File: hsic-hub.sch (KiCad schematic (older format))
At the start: 10 parts

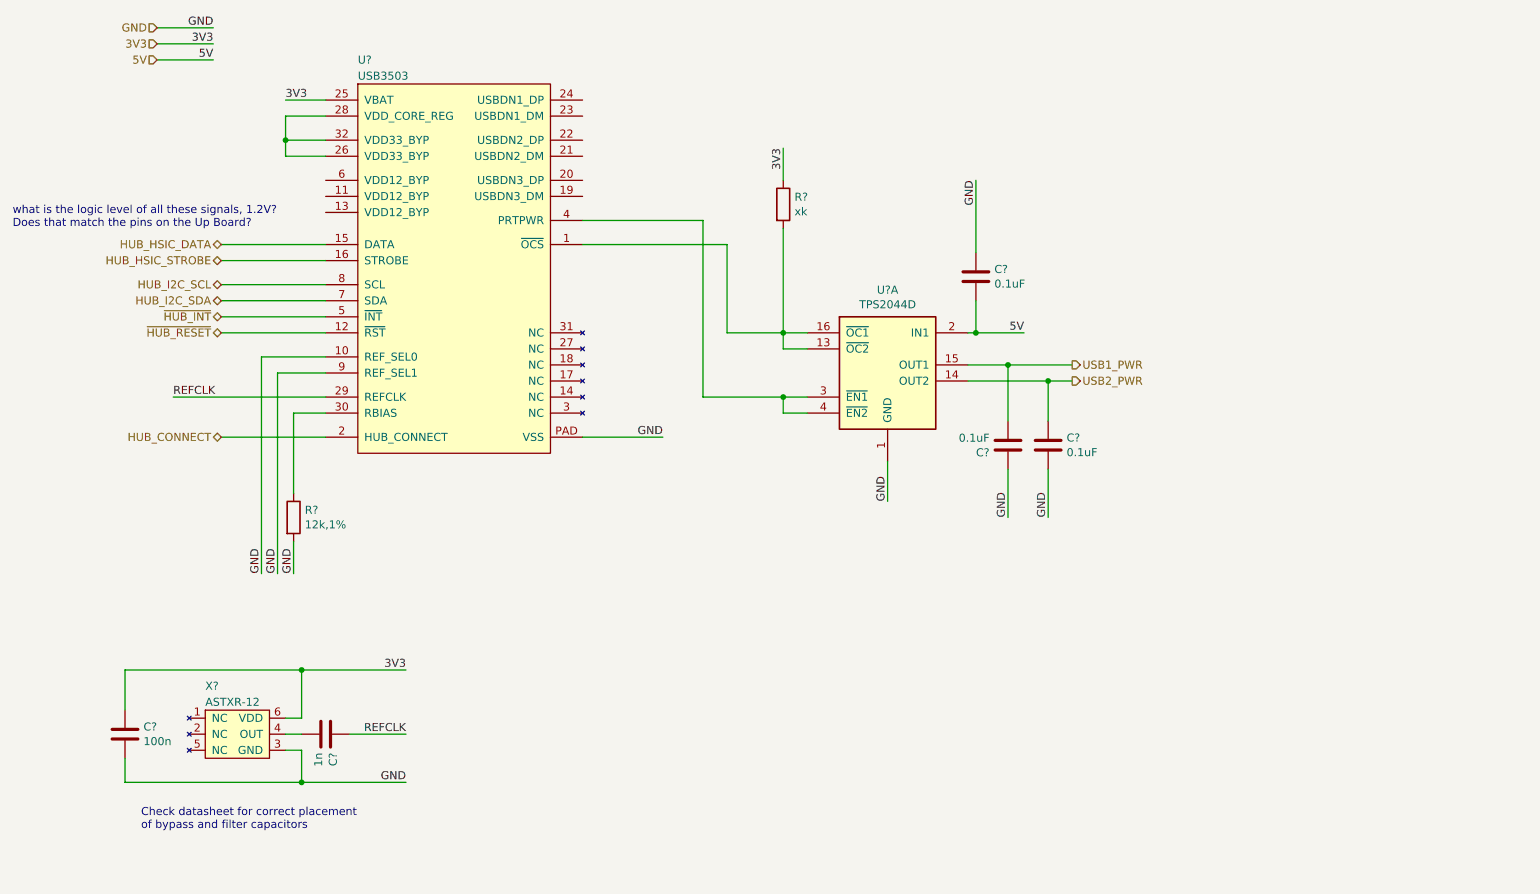
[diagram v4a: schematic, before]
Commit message: Add header for USB connector to libraries and schematic.
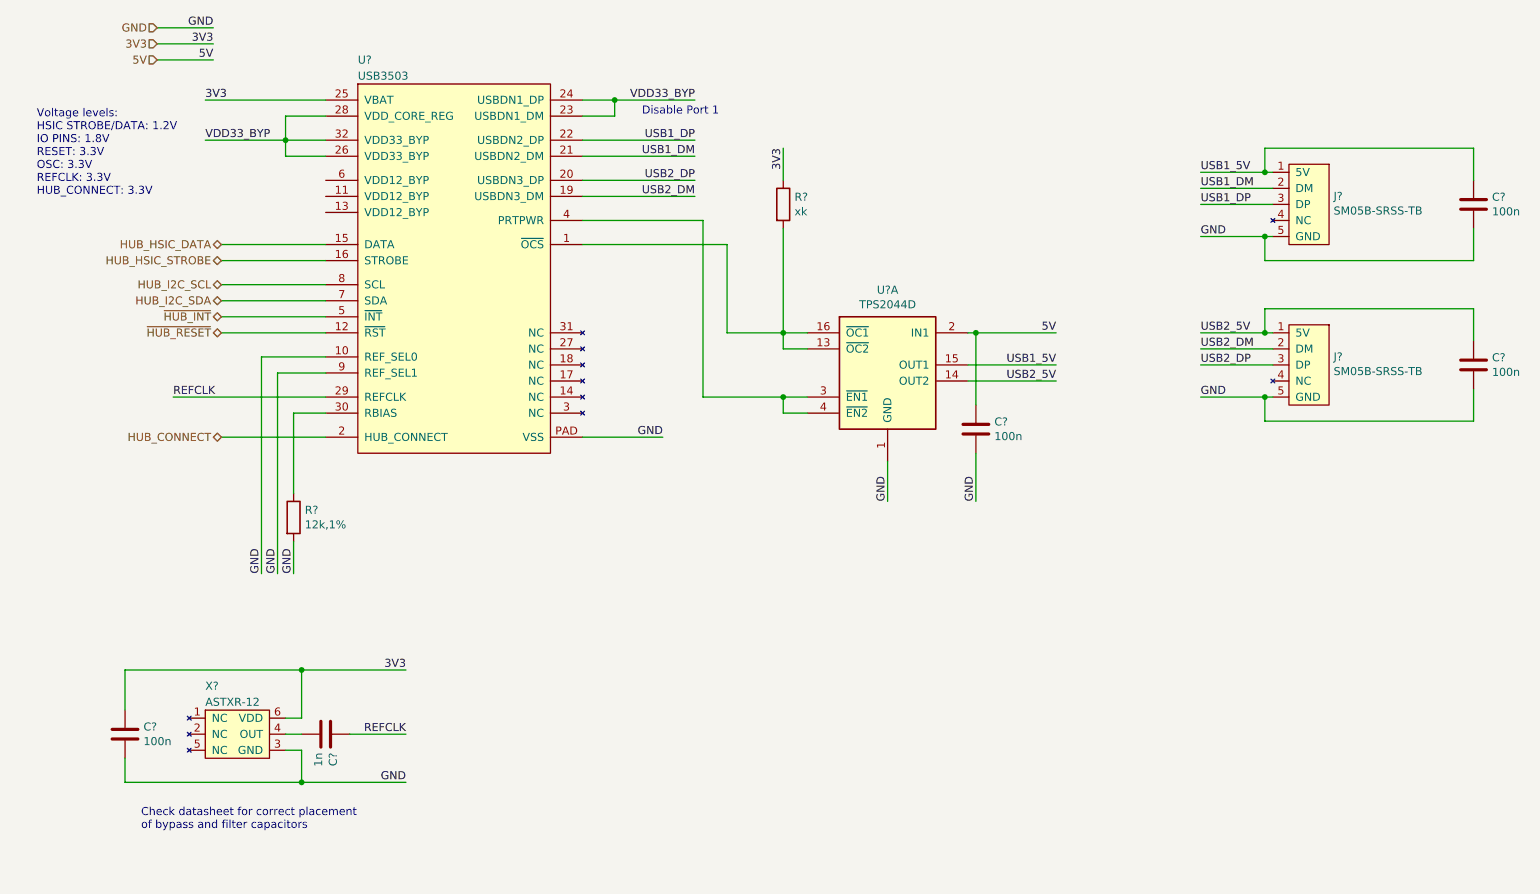
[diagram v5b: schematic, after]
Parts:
- removed C?: 0.1uF, symbol Device:C
- added C?: 100n, symbol Device:C
- added J? (x2): SM05B-SRSS-TB, Drone:SM05B-SRSS-TB, symbol Drone:SM05B-SRSS-TB
- C? (x2): value 0.1uF -> 100n
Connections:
- net 5V: now also C?.1; no longer C?.2
- net GND: now also C?.2, C?.2, J?.5 (GND), J?.5 (GND); no longer C?.1
- net USB2_DM: now reaches U?.19 (USBDN3_DM)
- net USB2_DM: now also J?.2 (DM)
- net USB2_DP: now reaches U?.20 (USBDN3_DP)
- net USB2_DP: now also J?.3 (DP)
- net USB1_DM: now reaches U?.21 (USBDN2_DM)
- net USB1_DM: now also J?.2 (DM)
- net USB1_DP: now reaches U?.22 (USBDN2_DP)
- net USB1_DP: now also J?.3 (DP)
- net VDD33_BYP: now reaches U?.23 (USBDN1_DM)
- net VDD33_BYP: now also U?.24 (USBDN1_DP), U?.26 (VDD33_BYP), U?.28 (VDD_CORE_REG), U?.32 (VDD33_BYP)
- net USB1_PWR renamed USB1_5V
- net USB1_5V: now also C?.1, J?.1 (5V)
- net USB2_PWR renamed USB2_5V
- net USB2_5V: now also C?.1, J?.1 (5V); no longer C?.1
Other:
- note added: "Disable Port 1"
- note added: "Voltage levels:\nHSIC STROBE/DATA: 1.2V\nIO PINS: 1.8V\nRESET: 3.3V\nOSC: 3.3V\nREFCLK: 3.3V\nHUB_CONNECT: 3.3V\n"
- note removed: "what is the logic level of all these signals, 1.2V?\nDoes that match the pins on the Up Board?"
- moved on the sheet: C?
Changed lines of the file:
@@
 Wire Wire Line
 	2200 1450 2200 1550
-Text Label 2200 1200 0    50   ~ 0
-3V3
-Wire Wire Line
-	2450 1200 2200 1200
+Text Label 1700 1200 0    50   ~ 0
+3V3
+Wire Wire Line
+	2450 1200 1700 1200
 Text HLabel 1400 850  0    50   Input ~ 0
 3V3
@@
 Wire Wire Line
 	1400 950  1750 950
-Wire Wire Line
-	6800 2650 6500 2650
-Text Label 6800 2650 2    50   ~ 0
+Text Label 7000 2650 2    50   ~ 0
 5V
 Wire Wire Line
@@
 L Device:C C?
 U 1 1 5E332CF8
-P 6500 2300
-F 0 "C?" H 6615 2346 50  0000 L CNN
-F 1 "0.1uF" H 6615 2255 50  0000 L CNN
-F 2 "" H 6538 2150 50  0001 C CNN
-F 3 "~" H 6500 2300 50  0001 C CNN
-	1    6500 2300
-	1    0    0    -1
-$EndComp
-Text Label 6500 1700 3    50   ~ 0
-GND
-Wire Wire Line
-	6500 1700 6500 2150
-Wire Wire Line
-	6500 2450 6500 2650
-Connection ~ 6500 2650
-Wire Wire Line
-	6500 2650 6450 2650
-Text HLabel 7100 2850 2    50   Output ~ 0
-USB1_PWR
-Text HLabel 7100 2950 2    50   Output ~ 0
-USB2_PWR
-Wire Wire Line
-	6450 2850 6700 2850
-Wire Wire Line
-	6450 2950 6950 2950
-Text Label 6700 3800 1    50   ~ 0
-GND
-Wire Wire Line
-	6700 3500 6700 3800
-Text Label 6950 3800 1    50   ~ 0
-GND
-Wire Wire Line
-	6950 3500 6950 3800
-Wire Wire Line
-	6950 2950 6950 3200
-Connection ~ 6950 2950
-Wire Wire Line
-	6950 2950 7100 2950
-Wire Wire Line
-	6700 2850 6700 3200
-Connection ~ 6700 2850
-Wire Wire Line
-	6700 2850 7100 2850
-$Comp
-L Device:C C?
-U 1 1 5E3408C5
-P 6950 3350
-F 0 "C?" H 7065 3396 50  0000 L CNN
-F 1 "0.1uF" H 7065 3305 50  0000 L CNN
-F 2 "" H 6988 3200 50  0001 C CNN
-F 3 "~" H 6950 3350 50  0001 C CNN
-	1    6950 3350
-	1    0    0    -1
-$EndComp
-$Comp
-L Device:C C?
-U 1 1 5E340CE5
-P 6700 3350
-F 0 "C?" H 6815 3396 50  0000 L CNN
-F 1 "0.1uF" H 6815 3305 50  0000 L CNN
-F 2 "" H 6738 3200 50  0001 C CNN
-F 3 "~" H 6700 3350 50  0001 C CNN
-	1    6700 3350
-	-1   0    0    1
-$EndComp
+P 6500 3250
+F 0 "C?" H 6615 3296 50  0000 L CNN
+F 1 "100n" H 6615 3205 50  0000 L CNN
+F 2 "" H 6538 3100 50  0001 C CNN
+F 3 "~" H 6500 3250 50  0001 C CNN
+	1    6500 3250
+	1    0    0    -1
+$EndComp
+Text Label 6500 3700 1    50   ~ 0
+GND
 Text Label 5300 1500 3    50   ~ 0
 3V3
@@
 	1    0    0    -1
 $EndComp
-Text Notes 500  2000 0    50   ~ 0
-what is the logic level of all these signals, 1.2V?\nDoes that match the pins on the Up Board?
+Text Notes 650  1800 0    50   ~ 0
+Voltage levels:\nHSIC STROBE/DATA: 1.2V\nIO PINS: 1.8V\nRESET: 3.3V\nOSC: 3.3V\nREFCLK: 3.3V\nHUB_CONNECT: 3.3V\n
 Text Label 2950 4750 2    50   ~ 0
 3V3
@@
 Text Notes 1300 5750 0    50   ~ 0
 Check datasheet for correct placement\nof bypass and filter capacitors
+Text Label 1700 1450 0    50   ~ 0
+VDD33_BYP
+Wire Wire Line
+	1700 1450 2200 1450
+Text Label 4750 1200 2    50   ~ 0
+VDD33_BYP
+Wire Wire Line
+	4050 1200 4250 1200
+Wire Wire Line
+	4050 1300 4250 1300
+Wire Wire Line
+	4250 1300 4250 1200
+Wire Wire Line
+	4250 1200 4750 1200
+Connection ~ 4250 1200
+Text Notes 4900 1300 2    50   ~ 0
+Disable Port 1
+$Comp
+L Drone:SM05B-SRSS-TB J?
+U 1 1 5E385FFC
+P 8550 1600
+F 0 "J?" H 8372 1401 50  0000 R CNN
+F 1 "SM05B-SRSS-TB" H 8372 1310 50  0000 R CNN
+F 2 "Drone:SM05B-SRSS-TB" H 8400 1850 50  0001 L CNN
+F 3 "" H 8550 1600 50  0001 C CNN
+	1    8550 1600
+	-1   0    0    -1
+$EndComp
+$Comp
+L Device:C C?
+U 1 1 5E3408C5
+P 9600 1850
+F 0 "C?" H 9715 1896 50  0000 L CNN
+F 1 "100n" H 9715 1805 50  0000 L CNN
+F 2 "" H 9638 1700 50  0001 C CNN
+F 3 "~" H 9600 1850 50  0001 C CNN
+	1    9600 1850
+	1    0    0    -1
+$EndComp
+Wire Wire Line
+	6450 2850 7000 2850
+Wire Wire Line
+	6450 2950 7000 2950
+Text Label 7900 1750 0    50   ~ 0
+USB1_DM
+Text Label 7900 1850 0    50   ~ 0
+USB1_DP
+Wire Wire Line
+	6450 2650 6500 2650
+Wire Wire Line
+	6500 3100 6500 2650
+Connection ~ 6500 2650
+Wire Wire Line
+	6500 2650 7000 2650
+Wire Wire Line
+	6500 3400 6500 3700
+Text Label 7000 2850 2    50   ~ 0
+USB1_5V
+Text Label 7000 2950 2    50   ~ 0
+USB2_5V
+Text Label 7900 1650 0    50   ~ 0
+USB1_5V
+Text Label 7900 2050 0    50   ~ 0
+GND
+Wire Wire Line
+	7900 2050 8300 2050
+Wire Wire Line
+	7900 1850 8350 1850
+Wire Wire Line
+	7900 1750 8350 1750
+Wire Wire Line
+	7900 1650 8300 1650
+Wire Wire Line
+	8300 1650 8300 1500
+Wire Wire Line
+	8300 1500 9600 1500
+Wire Wire Line
+	9600 1500 9600 1700
+Connection ~ 8300 1650
+Wire Wire Line
+	8300 1650 8350 1650
+Wire Wire Line
+	9600 2000 9600 2200
+Wire Wire Line
+	9600 2200 8300 2200
+Wire Wire Line
+	8300 2200 8300 2050
+Connection ~ 8300 2050
+Wire Wire Line
+	8300 2050 8350 2050
+$Comp
+L Drone:SM05B-SRSS-TB J?
+U 1 1 5E3AC9C2
+P 8550 2600
+F 0 "J?" H 8372 2401 50  0000 R CNN
+F 1 "SM05B-SRSS-TB" H 8372 2310 50  0000 R CNN
+F 2 "Drone:SM05B-SRSS-TB" H 8400 2850 50  0001 L CNN
+F 3 "" H 8550 2600 50  0001 C CNN
+	1    8550 2600
+	-1   0    0    -1
+$EndComp
+$Comp
+L Device:C C?
+U 1 1 5E3AC9C8
+P 9600 2850
+F 0 "C?" H 9715 2896 50  0000 L CNN
+F 1 "100n" H 9715 2805 50  0000 L CNN
+F 2 "" H 9638 2700 50  0001 C CNN
+F 3 "~" H 9600 2850 50  0001 C CNN
+	1    9600 2850
+	1    0    0    -1
+$EndComp
+Text Label 7900 2750 0    50   ~ 0
+USB2_DM
+Text Label 7900 2850 0    50   ~ 0
+USB2_DP
+Text Label 7900 2650 0    50   ~ 0
+USB2_5V
+Text Label 7900 3050 0    50   ~ 0
+GND
+Wire Wire Line
+	7900 3050 8300 3050
+Wire Wire Line
+	7900 2850 8350 2850
+Wire Wire Line
+	7900 2750 8350 2750
+Wire Wire Line
+	7900 2650 8300 2650
+Wire Wire Line
+	8300 2650 8300 2500
+Wire Wire Line
+	8300 2500 9600 2500
+Wire Wire Line
+	9600 2500 9600 2700
+Connection ~ 8300 2650
+Wire Wire Line
+	8300 2650 8350 2650
+Wire Wire Line
+	9600 3000 9600 3200
+Wire Wire Line
+	9600 3200 8300 3200
+Wire Wire Line
+	8300 3200 8300 3050
+Connection ~ 8300 3050
+Wire Wire Line
+	8300 3050 8350 3050
+Text Label 4750 1550 2    50   ~ 0
+USB1_DM
+Text Label 4750 1450 2    50   ~ 0
+USB1_DP
+Wire Wire Line
+	4050 1450 4750 1450
+Wire Wire Line
+	4050 1550 4750 1550
+Text Label 4750 1800 2    50   ~ 0
+USB2_DM
+Text Label 4750 1700 2    50   ~ 0
+USB2_DP
+Wire Wire Line
+	4050 1700 4750 1700
+Wire Wire Line
+	4050 1800 4750 1800
 $EndSCHEMATC

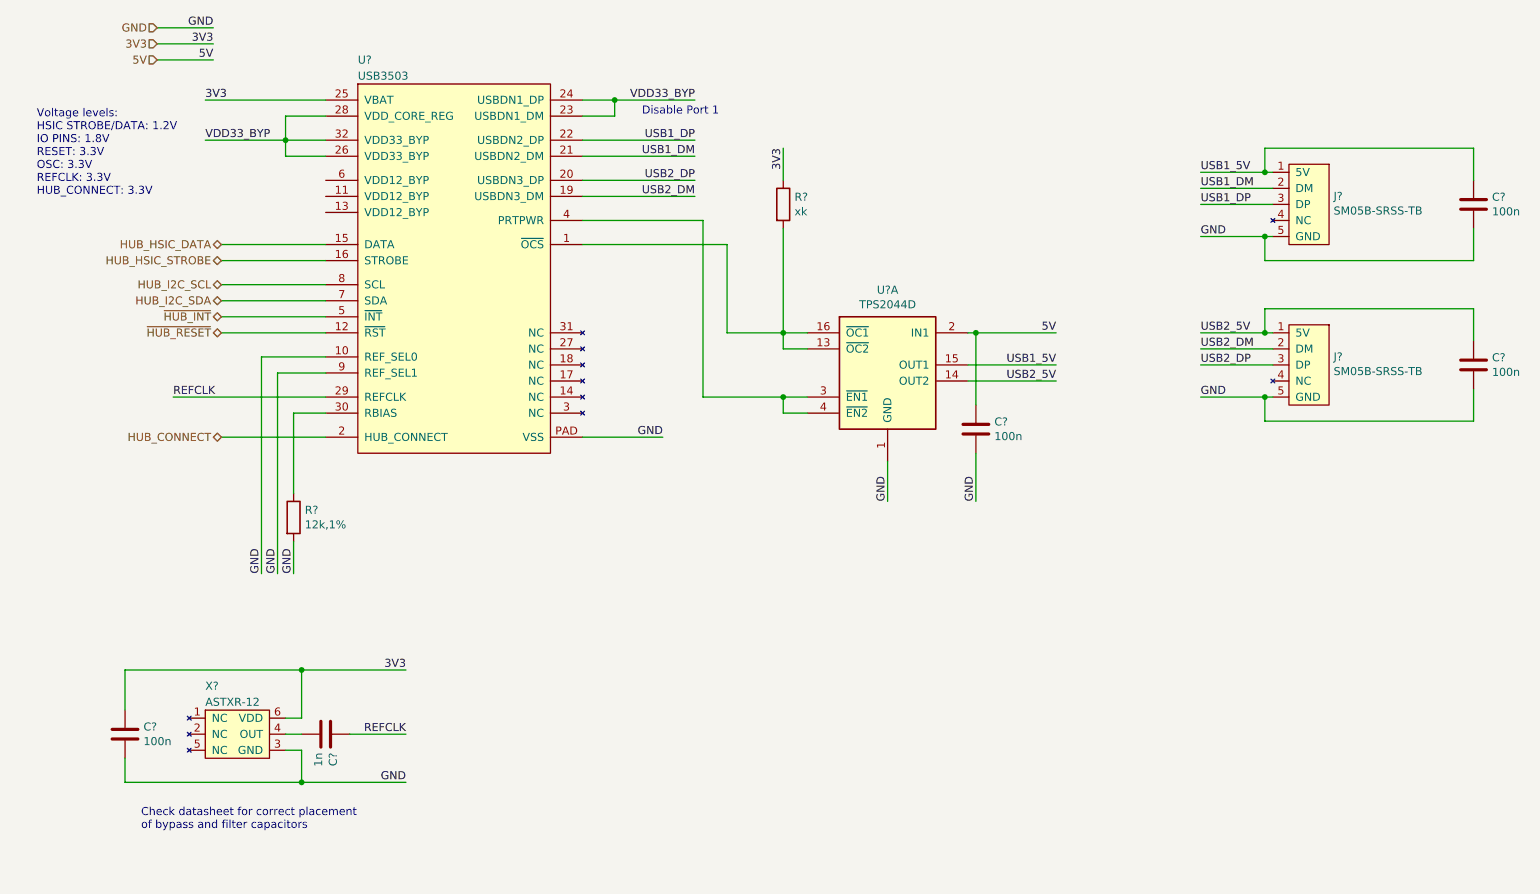
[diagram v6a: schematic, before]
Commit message: Add TPS2054D and update HSIC schematic.
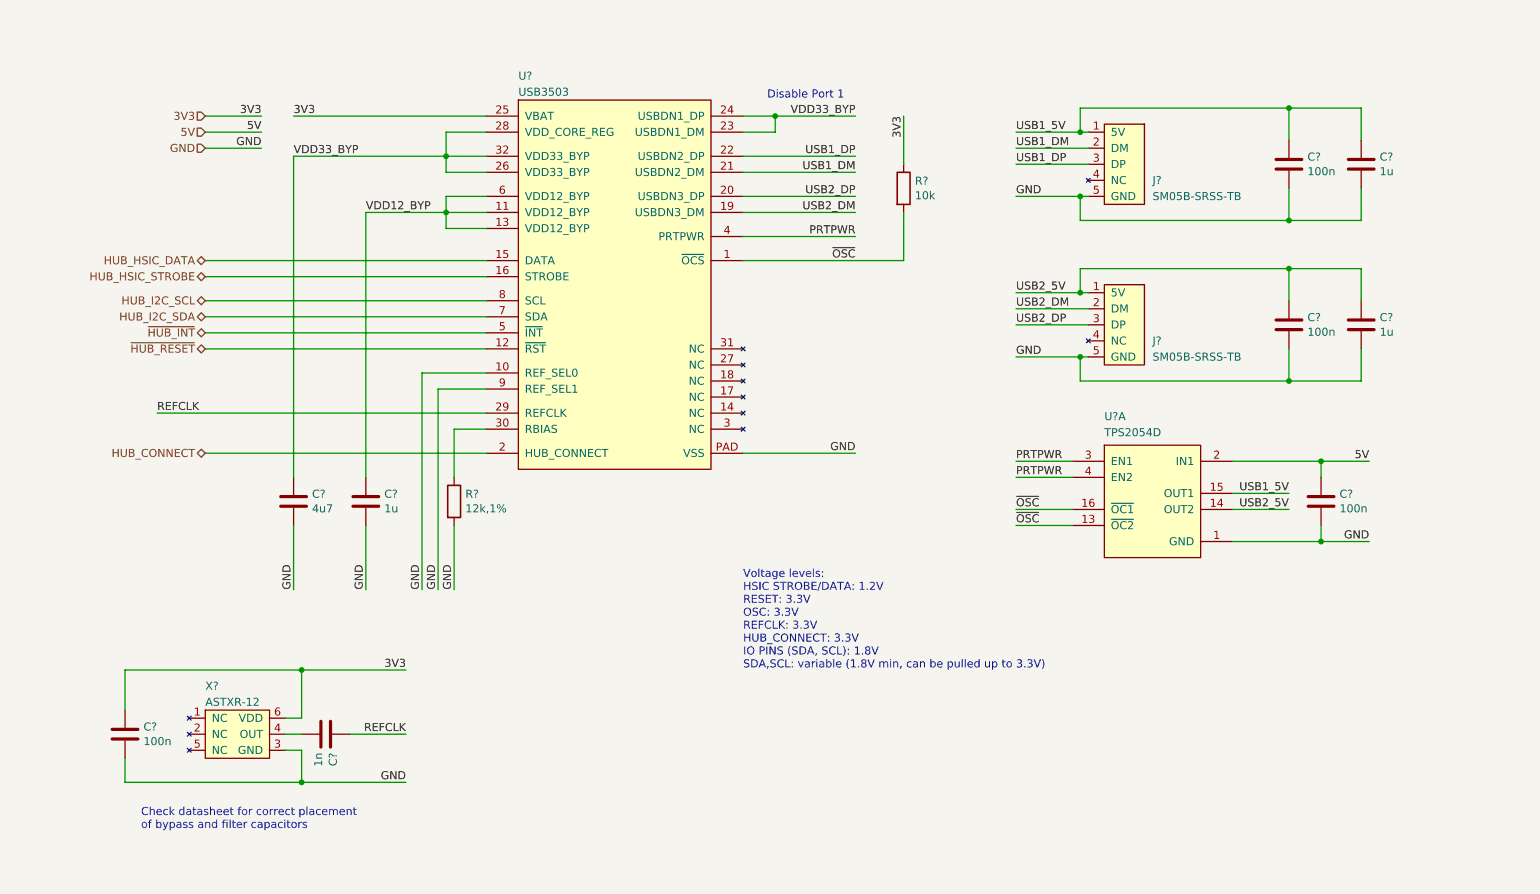
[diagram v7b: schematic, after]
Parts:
- removed U?: TPS2044D, Package_SO:SOIC-16_3.9x9.9mm_P1.27mm, symbol Power_Management:TPS2044D
- added C? (x3): 1u, symbol Device:C
- added C?: 4u7, symbol Device:C
- added U?: TPS2054D, Package_SO:SOIC-16_3.9x9.9mm_P1.27mm, symbol Drone:TPS2054D
- R?: value xk -> 10k
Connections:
- net 5V: now also U?.2 (IN1)
- net GND: now also C?.2, C?.2, C?.2, C?.2, U?.1 (GND)
- net USB1_5V: now also C?.1, U?.15 (OUT1)
- net USB2_5V: now also C?.1, U?.14 (OUT2)
- net VDD33_BYP: now also C?.1
- net ~OSC: now reaches R?.2, U?.1 (~OCS)
- net ~OSC: now also U?.13 (~OC2), U?.16 (~OC1)
- net VDD12_BYP: now reaches U?.11 (VDD12_BYP)
- net VDD12_BYP: now also U?.13 (VDD12_BYP), U?.6 (VDD12_BYP), C?.1
- net PRTPWR: now reaches U?.4 (PRTPWR)
- net PRTPWR: now also U?.3 (EN1), U?.4 (EN2)
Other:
- note added: "Voltage levels:\nHSIC STROBE/DATA: 1.2V\nRESET: 3.3V\nOSC: 3.3V\nREFCLK: 3.3V\nHUB_CONNECT: 3.3V\nIO PINS (SDA, SCL): 1.8V\nSDA,SCL: variable (1.8V min, can be pulled up to 3.3V)"
- note removed: "Voltage levels:\nHSIC STROBE/DATA: 1.2V\nIO PINS: 1.8V\nRESET: 3.3V\nOSC: 3.3V\nREFCLK: 3.3V\nHUB_CONNECT: 3.3V\n"
- moved on the sheet: C?, J?, R?, U?
